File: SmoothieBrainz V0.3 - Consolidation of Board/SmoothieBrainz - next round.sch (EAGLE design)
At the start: 189 parts, among them IC1 LPC1769, IC5 LD117ADT33TR, Q1 BSL207SP, Q2 12MHz, SW1 SW_TACT_4P_B, SW3 SW_TACT_4P_B, U2 HC_05, U3 USD-SOCKETUSD, X1 GMSTBV2, X14 USBPTH, X2 MSTBA2, X3 MSTBA4, X4 1751248, X5 1751248, X6 1751248, X7 1751248, X8 1751248

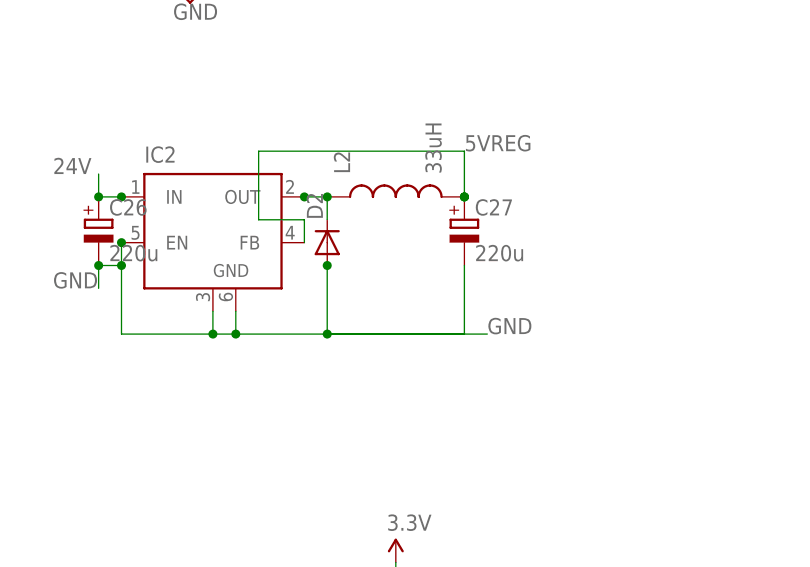
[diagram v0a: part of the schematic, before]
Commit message: partial motor routing, better ground for stepstick sockets
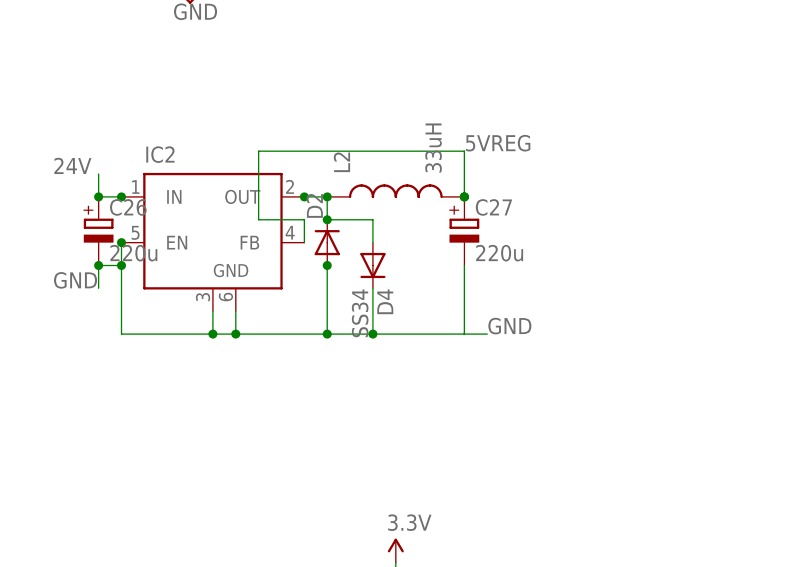
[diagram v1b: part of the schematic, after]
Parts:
- added D4: SS34, Fairchild Rectifier Diodes s3x_10:S3A
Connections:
- net GND: now also D4.C
- net N$9: now also D4.A
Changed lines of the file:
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@@
 <part name="LED11" library="led" deviceset="LED" device="SML0805"/>
 <part name="R48" library="resistor" deviceset="R-EU_" device="R0603" value="1.5k"/>
+<part name="D4" library="Fairchild Rectifier Diodes s3x_10" deviceset="S3*" device="" technology="A" value="SS34"/>
 </parts>
 <sheets>
@@
 <instance part="LED11" gate="G$1" x="492.76" y="236.22" rot="MR270"/>
 <instance part="R48" gate="G$1" x="510.54" y="236.22" rot="MR180"/>
+<instance part="D4" gate="G$1" x="314.96" y="317.5" rot="R270"/>
 </instances>
 <busses>
@@
 <wire x1="287.02" y1="317.5" x2="284.48" y2="317.5" width="0.1524" layer="91"/>
 <wire x1="284.48" y1="317.5" x2="284.48" y2="314.96" width="0.1524" layer="91"/>
-<wire x1="309.88" y1="309.88" x2="325.12" y2="309.88" width="0.1524" layer="91"/>
-<wire x1="309.88" y1="309.88" x2="327.66" y2="309.88" width="0.1524" layer="91"/>
+<wire x1="314.96" y1="309.88" x2="325.12" y2="309.88" width="0.1524" layer="91"/>
+<wire x1="309.88" y1="309.88" x2="314.96" y2="309.88" width="0.1524" layer="91"/>
 <label x="327.66" y="309.88" size="1.778" layer="95"/>
 <junction x="287.02" y="317.5"/>
@@
 <junction x="284.48" y="317.5"/>
 <pinref part="C27" gate="G$1" pin="-"/>
+<wire x1="325.12" y1="309.88" x2="327.66" y2="309.88" width="0.1524" layer="91"/>
 <wire x1="325.12" y1="317.5" x2="325.12" y2="309.88" width="0.1524" layer="91"/>
+<pinref part="D4" gate="G$1" pin="C"/>
+<wire x1="314.96" y1="314.96" x2="314.96" y2="309.88" width="0.1524" layer="91"/>
+<junction x="314.96" y="309.88"/>
 </segment>
 <segment>
@@
 <junction x="309.88" y="325.12"/>
 <junction x="307.34" y="325.12"/>
-</segment>
-</net>
+<pinref part="D4" gate="G$1" pin="A"/>
+<wire x1="314.96" y1="320.04" x2="314.96" y2="322.58" width="0.1524" layer="91"/>
+<wire x1="314.96" y1="322.58" x2="309.88" y2="322.58" width="0.1524" layer="91"/>
+<junction x="309.88" y="322.58"/>
+</segment>
+</net>

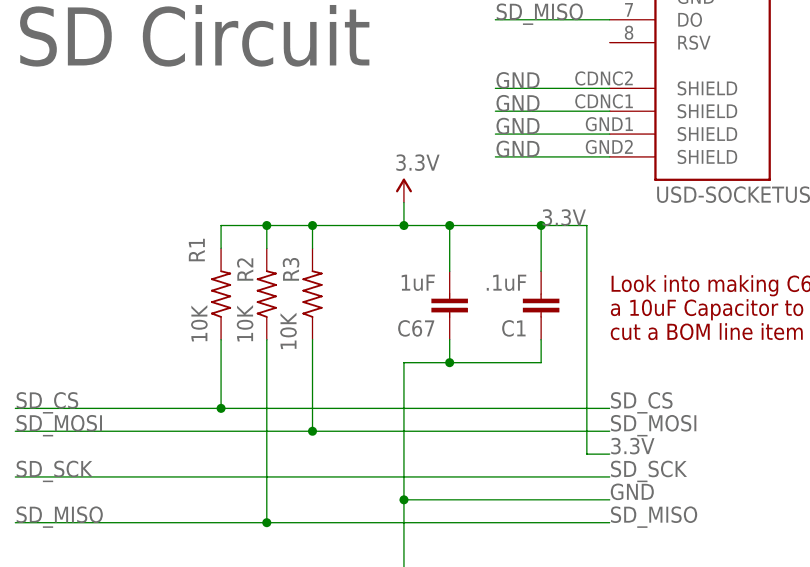
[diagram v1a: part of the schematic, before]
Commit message: Changed 1uF Capacitor near SD card to 10uf
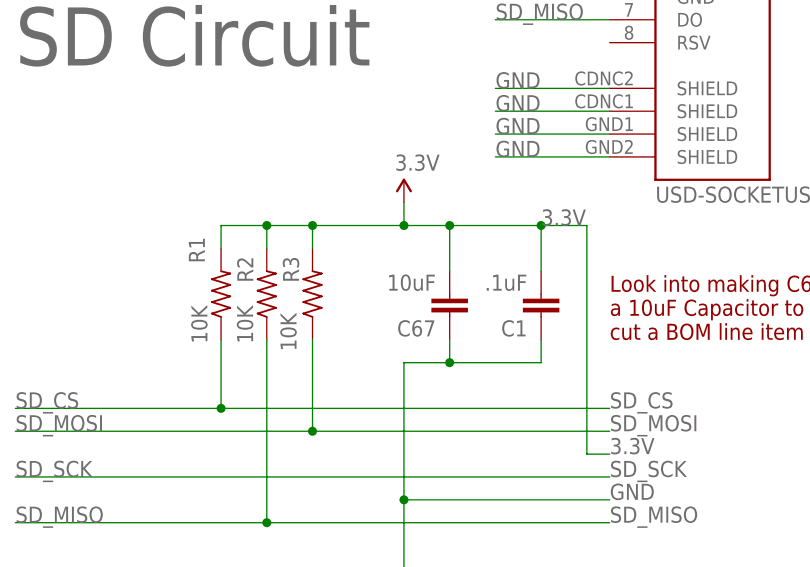
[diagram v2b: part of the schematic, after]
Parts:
- C67: value 1uF -> 10uF
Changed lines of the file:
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@@
 <part name="AGND1" library="supply1" deviceset="AGND" device=""/>
 <part name="AGND2" library="supply1" deviceset="AGND" device=""/>
-<part name="C67" library="resistor" deviceset="C-EU" device="C0603" value="1uF"/>
+<part name="C67" library="resistor" deviceset="C-EU" device="C0603" value="10uF"/>
 <part name="X14" library="SparkFun" deviceset="USB" device="PTH"/>
 <part name="SJ1" library="SparkFun" deviceset="SOLDERJUMPER_2WAY" device="S"/>

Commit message: added onboard Ethernet, now need to reposition LEDS and 3v3 reg
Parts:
- added C41, C42: 104, resistor:C-EUC0603
- added C43: 100uF, resistor:CPOL-EU153CLV-0605
- added C44, C46, C47, C51, C52, C53: .1uF, resistor:C-EUC0603
- added C45, C50: 10uF, SparkFun:CAP_POL1206
- added C48: 1uF, SparkFun:CAP_POL1206
- added C49: 470pF, resistor:C-EUC0603K
- added C54, C55, C56, C57: 18pF, resistor:C-EUC0603
- added C58, C59: 12pF, resistor:C-EUC0603
- added FB1: (no value), microbuilder:FERRITE
- added IC3: (no value), microbuilder:74LVC1G04
- added IC8: (no value), microbuilder:LAN8720
- added JP1: (no value), SparkFun-Connectors:M04POLAR_LOCK
- added JP3: (no value), SparkFun-Connectors:M04LOCK
- added Q3: 25MHz, microbuilder:CRYSTALTHIN
- added R49: 1k, resistor:R-EU_R0603
- added R50: 10k, resistor:R-EU_R0603
- added R51, R61: 330R, resistor:R-US_R0603
- added R52: 1.5K, resistor:R-US_R0603
- added R53, R58, R59, R60: 22R, resistor:R-US_R0603
- added R54, R62: 10K, resistor:R-US_R0603
- added R55, R56, R57, R65: 49.9R, resistor:R-US_R0603
- added R63: 12.1K, resistor:R-US_R0603
- added R64: 1M, resistor:R-US_R0603
- added RJ1: HR911105A, Itead_BP_110825.lbr:HR911105A
- added SJ20, SJ21, SJ22: (no value), jumper:SJ
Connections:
- removed net D25: R35.1, R36.2
- removed net D26: R40.1, R41.2
- removed net D27: R43.1, R44.2
- removed net D28: R46.1, R47.2
- new net 1A$5M: JP1.2, JP3.2, U$8.1A
- new net 1B$5M: JP1.1, JP3.1, U$8.1B
- new net 2A$5M: JP1.3, JP3.3, U$8.2A
- new net 2B$5M: JP1.4, JP3.4, U$8.2B
- new net LED1/REGOFF: IC8.LED1/REGOFF, RJ1.G+
- new net LED2/NINTSEL: IC8.LED2/NINTSEL, R62.2, RJ1.Y+
- new net N$43: U$8.RST, U$8.SLEEP
- new net N$44: R49.2, SJ20.1, SJ21.1, SJ22.1
- new net N$45: SJ20.2, U$8.MS1
- new net N$46: SJ21.2, U$8.MS2
- new net N$47: SJ22.2, U$8.MS3
- new net N$48: IC8.RXD0, R58.1
- new net N$49: IC3.A, IC8.NINT/REFCLKO
- new net N$50: IC3.Y, R53.1
- new net N$53: R61.2, RJ1.G-
- new net N$54: R51.2, RJ1.Y-
- new net N$55: IC8.RXD1, R59.1
- new net N$56: C45.+, C46.1, C47.1, C52.1, C53.1, FB1.P$2, IC8.VDD1A, IC8.VDD2A, R55.1, R56.1, R57.1, R65.1, RJ1.P4, RJ1.P5
- new net N$63: IC8.CRS_DV, R60.1
- new net N$67: C59.1, IC8.XTAL2, Q3.1, R64.2
- new net N$68: C58.1, IC8.XTAL1, Q3.2, R64.1
- new net N$69: IC8.RBIAS, R63.2
- new net N$82: C48.+, C49.1, IC8.VDDCR
- new net RD+: C56.1, IC8.RX+, R57.2, RJ1.RD+
- new net RD-: C57.1, IC8.RX-, R65.2, RJ1.RD-
- new net TD+: C54.1, IC8.TX+, R55.2, RJ1.TD+
- new net TD-: C55.1, IC8.TX-, R56.2, RJ1.TD-
- net 24V: now also C41.1, C43.+, U$8.VMOT
- net 3.3V: now also C42.1, C44.1, C50.+, C51.1, FB1.P$1, IC3.VCC, IC8.VDDIO, R49.1, R50.2, R52.2, R54.2, U$8.VDD
- net DIR5: now also U$8.DIR
- net EN5: now also R50.1, U$8.EN
- net ENET_CRS: now also R60.2
- net ENET_MDC: now also IC8.MDC
- net ENET_MDIO: now also IC8.MDIO, R52.1
- net ENET_REF_CLK: now also R53.2
- net ENET_RXD0: now also R58.2
- net ENET_RXD1: now also R59.2
- net ENET_RX_ER: now also IC8.RXER, R54.1
- net ENET_TXD0: now also IC8.TXD0
- net ENET_TXD1: now also IC8.TXD1
- net ENET_TX_EN: now also IC8.TXEN
- net GND: now also C41.2, C42.2, C43.-, C44.2, C45.-, C46.2, C47.2, C48.-, C49.2, C50.-, C51.2, C52.2, C53.2, C54.2, C55.2, C56.2, C57.2, C58.2, C59.2, D4.A, IC3.GND, IC8.GND, R51.1, R61.1, R62.1, R63.1, RJ1.GND, RJ1.SHIELD0, RJ1.SHIELD1, U$8.GND@0, U$8.GND@1; no longer D4.C
- net N$9: now also D4.C; no longer D4.A
- net P1_22-3RD-SMALL-FET: now also R43.1, R44.2
- net P1_23-3RD-LARGE-FET: now also R40.1, R41.2
- net P2.6_FAN_FET: now also R46.1, R47.2
- net P2.7_HOTEND_FET: now also R35.1, R36.2
- net RSTOUT: now also IC8.NRST
- net STP5: now also U$8.STEP
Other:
- note added: "ETHERNET"
- moved on the sheet: D4

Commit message: need to try movingover to 7.62mm connectors
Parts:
- added JP13, JP14, JP15, JP16: (no value), SparkFun-Connectors:M03LOCK
- added T1: (no value), transistor:BC817-40-NPN-SOT23-BEC
- C45, C48, C50: device SparkFun:CAP_POL1206 -> resistor:C-EUC0603
- FB1: value (none) -> 30 Ohm Ferrite
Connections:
- net 3.3V: now also C50.1; no longer C50.+
- net GND: now also C45.2, C48.2, C50.2; no longer C45.-, C48.-, C50.-
- net N$56: now also C45.1; no longer C45.+
- net N$82: now also C48.1; no longer C48.+
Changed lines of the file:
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@@
 <part name="SUPPLY47" library="supply2" deviceset="GND" device=""/>
 <part name="P+10" library="SparkFun" deviceset="3.3V" device=""/>
-<part name="FB1" library="microbuilder" deviceset="FERRITE" device=""/>
-<part name="C45" library="SparkFun" deviceset="CAP_POL" device="1206" value="10uF"/>
+<part name="FB1" library="microbuilder" deviceset="FERRITE" device="" value="30 Ohm Ferrite"/>
+<part name="C45" library="resistor" deviceset="C-EU" device="C0603" value="10uF"/>
 <part name="C46" library="resistor" deviceset="C-EU" device="C0603" value=".1uF"/>
 <part name="C47" library="resistor" deviceset="C-EU" device="C0603" value=".1uF"/>
 <part name="SUPPLY48" library="supply2" deviceset="GND" device=""/>
 <part name="P+14" library="SparkFun" deviceset="3.3V" device=""/>
-<part name="C50" library="SparkFun" deviceset="CAP_POL" device="1206" value="10uF"/>
+<part name="C50" library="resistor" deviceset="C-EU" device="C0603" value="10uF"/>
 <part name="C51" library="resistor" deviceset="C-EU" device="C0603" value=".1uF"/>
 <part name="SUPPLY49" library="supply2" deviceset="GND" device=""/>
-<part name="C48" library="SparkFun" deviceset="CAP_POL" device="1206" value="1uF"/>
+<part name="C48" library="resistor" deviceset="C-EU" device="C0603" value="1uF"/>
 <part name="C49" library="resistor" deviceset="C-EU" device="C0603K" value="470pF"/>
 <part name="C53" library="resistor" deviceset="C-EU" device="C0603" value=".1uF"/>
@@
 <part name="R57" library="resistor" deviceset="R-US_" device="R0603" value="49.9R"/>
 <part name="R65" library="resistor" deviceset="R-US_" device="R0603" value="49.9R"/>
+<part name="T1" library="transistor" deviceset="*-NPN-" device="SOT23-BEC" technology="BC817-40"/>
+<part name="JP13" library="SparkFun-Connectors" deviceset="M03" device="LOCK"/>
+<part name="JP14" library="SparkFun-Connectors" deviceset="M03" device="LOCK"/>
+<part name="JP15" library="SparkFun-Connectors" deviceset="M03" device="LOCK"/>
+<part name="JP16" library="SparkFun-Connectors" deviceset="M03" device="LOCK"/>
 </parts>
 <sheets>
@@
 <attribute name="VALUE" x="458.978" y="640.08" size="1.778" layer="96" rot="R270"/>
 </instance>
+<instance part="T1" gate="G$1" x="525.78" y="157.48"/>
+<instance part="JP13" gate="G$1" x="548.64" y="157.48"/>
+<instance part="JP14" gate="G$1" x="548.64" y="142.24"/>
+<instance part="JP15" gate="G$1" x="548.64" y="127"/>
+<instance part="JP16" gate="G$1" x="548.64" y="111.76"/>
 </instances>
 <busses>
@@
 <junction x="347.98" y="635"/>
 <pinref part="SUPPLY48" gate="GND" pin="GND"/>
-<pinref part="C45" gate="G$1" pin="-"/>
+<pinref part="C45" gate="G$1" pin="2"/>
 <pinref part="C47" gate="G$1" pin="2"/>
 <pinref part="C46" gate="G$1" pin="2"/>
@@
 <pinref part="SUPPLY49" gate="GND" pin="GND"/>
 <pinref part="C51" gate="G$1" pin="2"/>
-<pinref part="C50" gate="G$1" pin="-"/>
-<pinref part="C48" gate="G$1" pin="-"/>
+<pinref part="C50" gate="G$1" pin="2"/>
+<pinref part="C48" gate="G$1" pin="2"/>
 <pinref part="C49" gate="G$1" pin="2"/>
 </segment>
@@
 <pinref part="IC8" gate="G$1" pin="VDDIO"/>
 <pinref part="P+14" gate="G$1" pin="3.3V"/>
-<pinref part="C50" gate="G$1" pin="+"/>
+<pinref part="C50" gate="G$1" pin="1"/>
 <pinref part="C51" gate="G$1" pin="1"/>
 </segment>
@@
 <pinref part="IC8" gate="G$1" pin="VDDCR"/>
 <pinref part="C49" gate="G$1" pin="1"/>
-<pinref part="C48" gate="G$1" pin="+"/>
+<pinref part="C48" gate="G$1" pin="1"/>
 </segment>
 </net>
@@
 <pinref part="C47" gate="G$1" pin="1"/>
 <pinref part="C46" gate="G$1" pin="1"/>
-<pinref part="C45" gate="G$1" pin="+"/>
+<pinref part="C45" gate="G$1" pin="1"/>
 <pinref part="C52" gate="G$1" pin="1"/>
 <pinref part="R55" gate="G$1" pin="1"/>

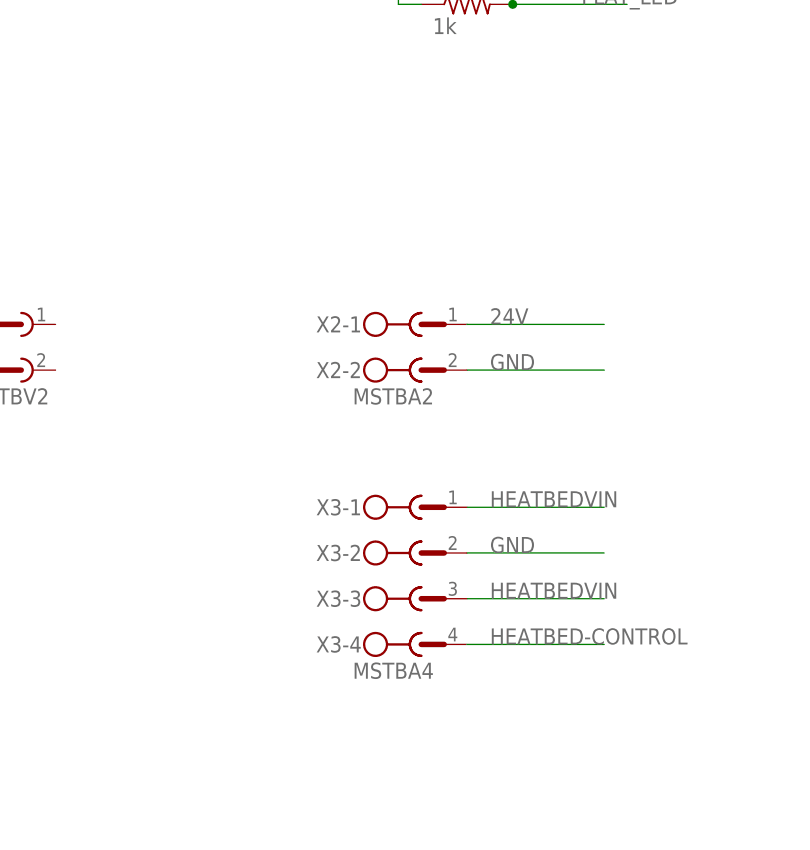
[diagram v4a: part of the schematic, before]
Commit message: switched to 7.62mm power terminals
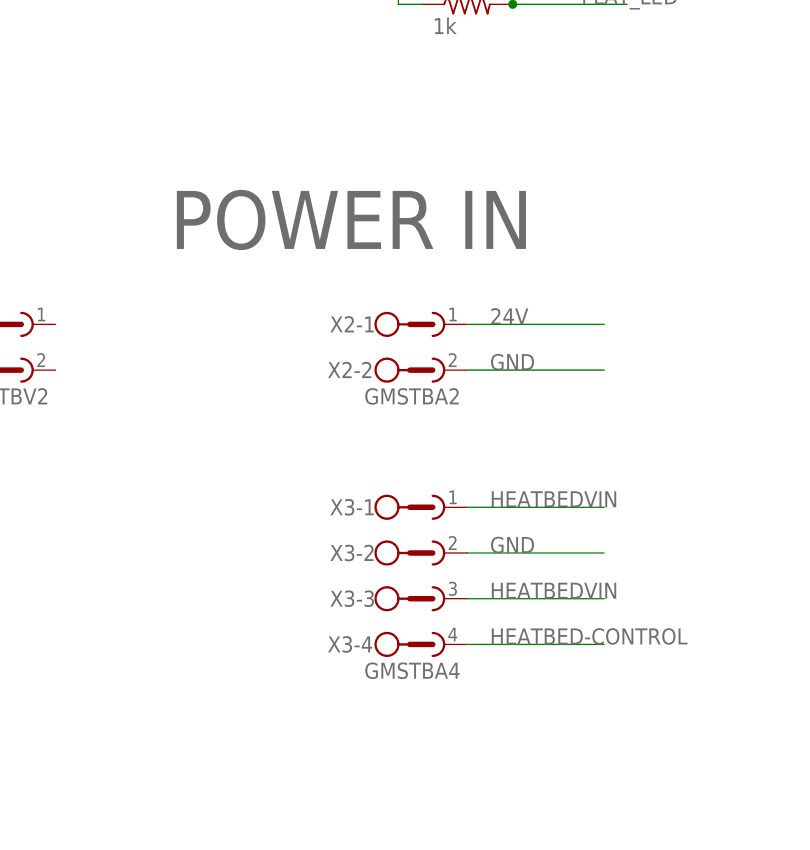
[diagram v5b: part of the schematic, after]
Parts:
- X2: value MSTBA2 -> GMSTBA2; device con-phoenix-508:MSTBA2 -> con-phoenix-762:GMSTBA2
- X3: value MSTBA4 -> GMSTBA4; device con-phoenix-508:MSTBA4 -> con-phoenix-762:GMSTBA4
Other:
- note added: "POWER IN"
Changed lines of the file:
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@@
 <part name="R32" library="resistor" deviceset="R-EU_" device="R0603" value="1.5k"/>
 <part name="LED6" library="led" deviceset="LED" device="SML0805"/>
-<part name="X2" library="con-phoenix-508" deviceset="MSTBA2" device=""/>
-<part name="X3" library="con-phoenix-508" deviceset="MSTBA4" device=""/>
+<part name="X2" library="con-phoenix-762" deviceset="GMSTBA2" device=""/>
+<part name="X3" library="con-phoenix-762" deviceset="GMSTBA4" device=""/>
 <part name="U$6" library="RepRapjr" deviceset="POLOLU_A4983CARRIER" device=""/>
 <part name="C35" library="resistor" deviceset="C-EU" device="C0603" value="104"/>
@@
 <text x="266.7" y="528.32" size="6.4516" layer="95">ETHERNET</text>
 <wire x1="591.82" y1="670.56" x2="591.82" y2="523.24" width="0.1524" layer="95"/>
+<text x="43.18" y="315.722" size="6.4516" layer="95">POWER IN</text>
 </plain>
 <instances>

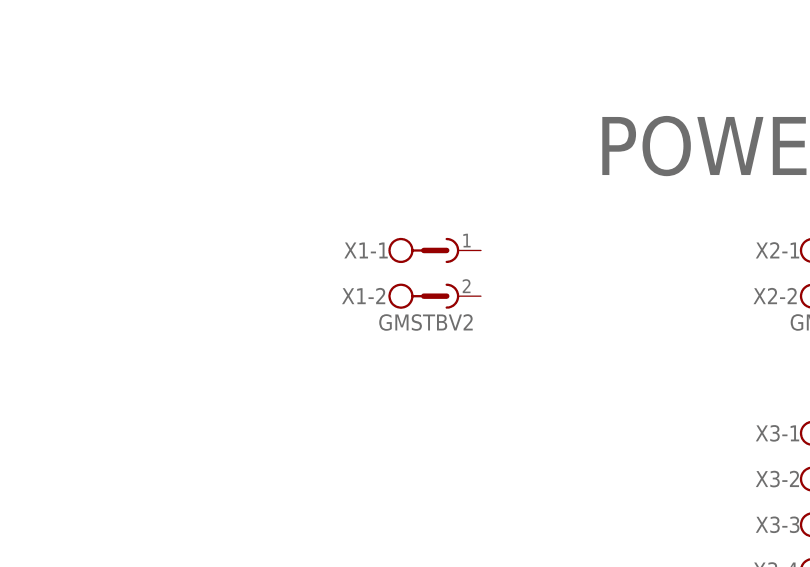
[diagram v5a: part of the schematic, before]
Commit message: replaced power conn with 7.62mm blocks, fixed heatbed mosfet pours
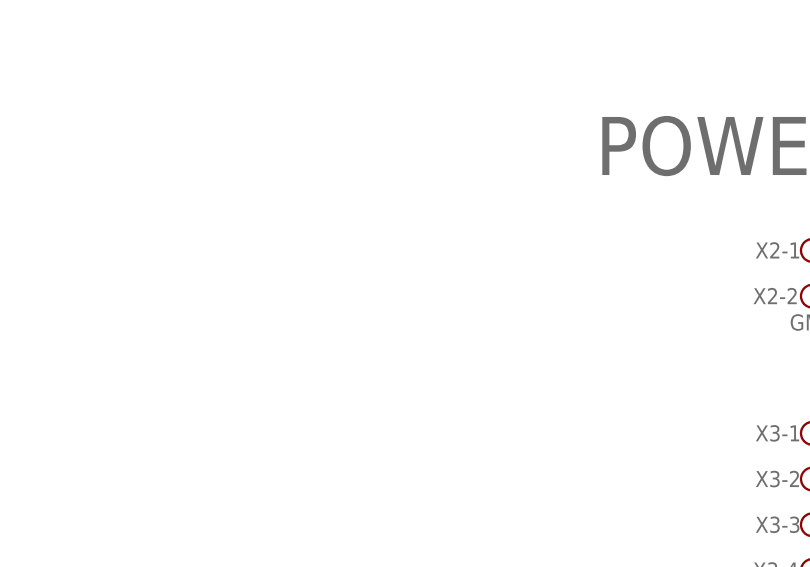
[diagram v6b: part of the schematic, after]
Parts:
- removed X1: GMSTBV2, con-phoenix-762:GMSTBV2
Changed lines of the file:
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@@
 <part name="R26" library="resistor" deviceset="R-EU_" device="R0603" value="10k"/>
 <part name="P+6" library="SparkFun" deviceset="3.3V" device=""/>
-<part name="X1" library="con-phoenix-762" deviceset="GMSTBV2" device=""/>
 <part name="U$10" library="Cohesion_parts" deviceset="N-POWER-MOSFET" device="D2PAK-MOSFET" value="SUM120N04-1M7L-GE3"/>
 <part name="R27" library="resistor" deviceset="R-EU_" device="R0603" value="10r"/>
@@
 <instance part="R26" gate="G$1" x="317.5" y="223.52" rot="R90"/>
 <instance part="P+6" gate="G$1" x="317.5" y="231.14"/>
-<instance part="X1" gate="-1" x="25.4" y="307.34"/>
-<instance part="X1" gate="-2" x="25.4" y="302.26"/>
 <instance part="U$10" gate="G$1" x="546.1" y="365.76"/>
 <instance part="R27" gate="G$1" x="525.78" y="363.22"/>
